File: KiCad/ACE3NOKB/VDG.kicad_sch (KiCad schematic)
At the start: 40 parts, among them Q101 2N3904

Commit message: First complete system. Unlikely to work but will serve as the basis of a system to test VGA.
Signed-off-by: John Bradley <flypie@rocketmail.com>
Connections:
- net INVERTCHAR: now reaches RN1.9 (R8.2), Z20.13, Z5-6.17 (D7)
- net ~{IN_VBI_OR_HBI}: now reaches Z19.4, Z20.12, Z20.6
- net SHIFT/~{LOAD}: now reaches Z19.6, Z28.15 (PE)
- net PIXEL: now reaches Z23.13, Z28.13 (Qh)
- net 50Hz renamed V_SYNC_PULSE(50Hz)
- net ENDOFSCR renamed SCREENY5
- net EOL renamed SCREENX5
- net HSYNC renamed H_SYNC_PULSE
- net SYNCLEVEL renamed ~{SYNC_PULSE}
- net VIDACTIVEONBUS renamed LOAD_SHIFT_REG
- net ~{CPUVDGRAMRD} renamed ~{CPUVDGRD}
- net ~{CPUVDGRAMWR} renamed ~{CPUVDGWR}
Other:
- note added: "END_OF_PIX_V"
- note removed: "50Hz"
- note removed: "VSYNC"
- moved on the sheet: AIN1, C3, D1, D11, Q101, R100, R132, R133, R134, R135, R136, R19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

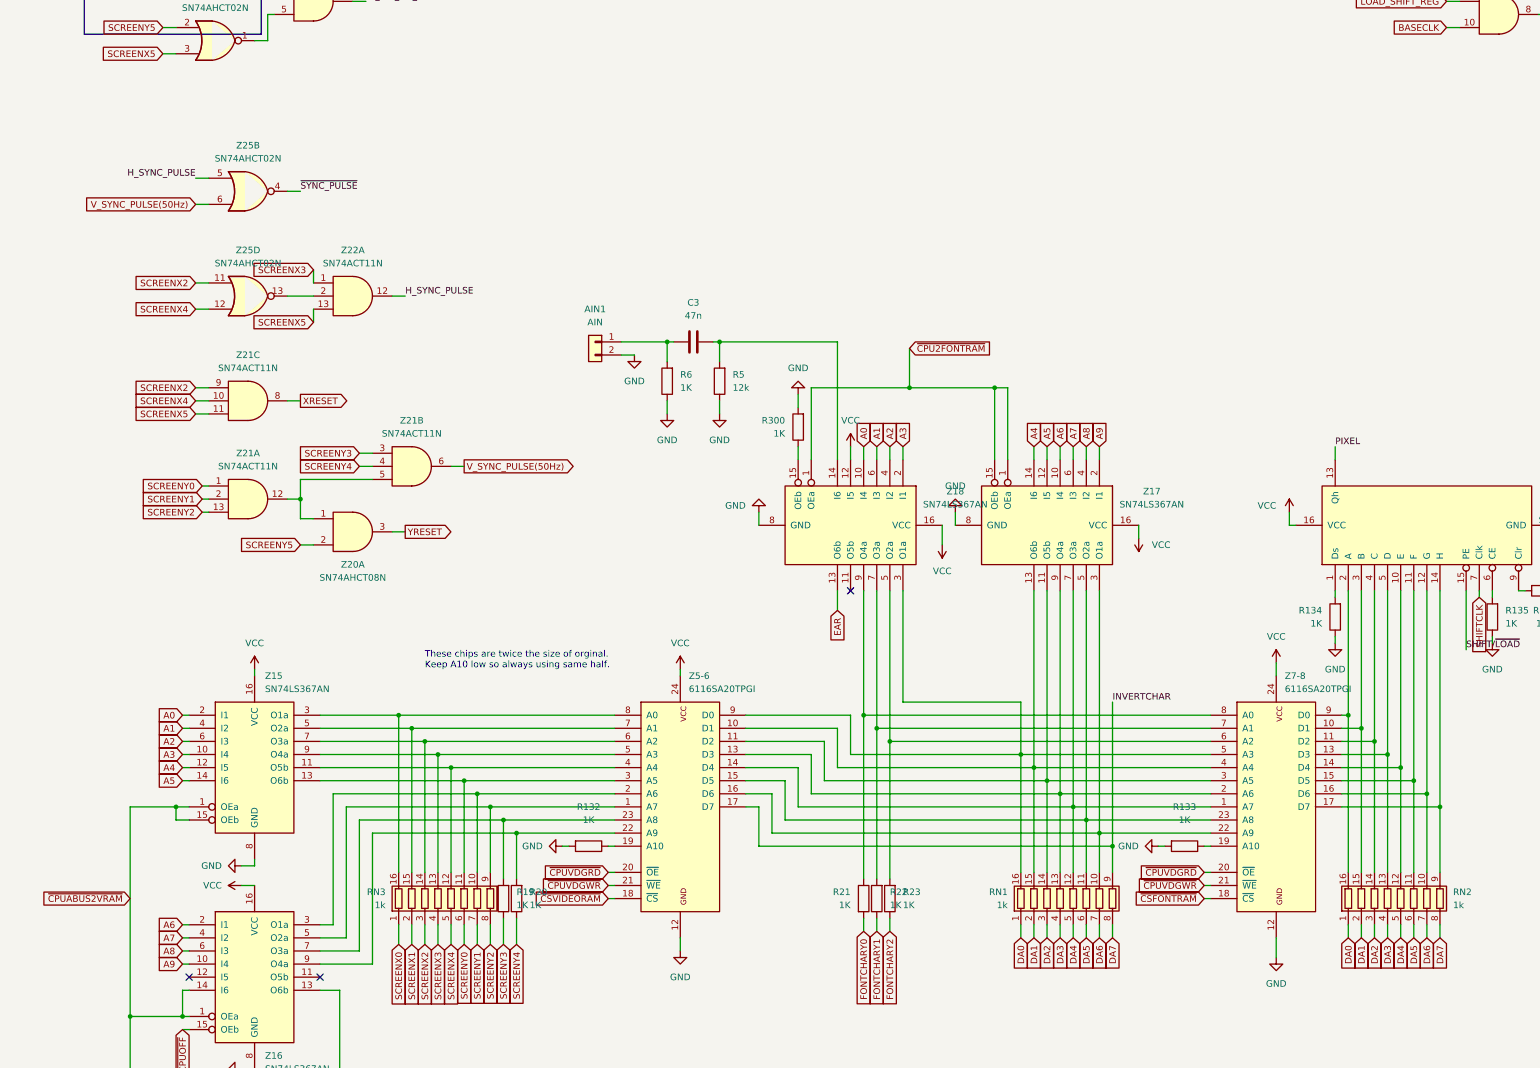
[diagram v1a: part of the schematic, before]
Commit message: Update to latest symbols. Change name of Data Bus from DA to D.
Signed-off-by: John Bradley <flypie@rocketmail.com>
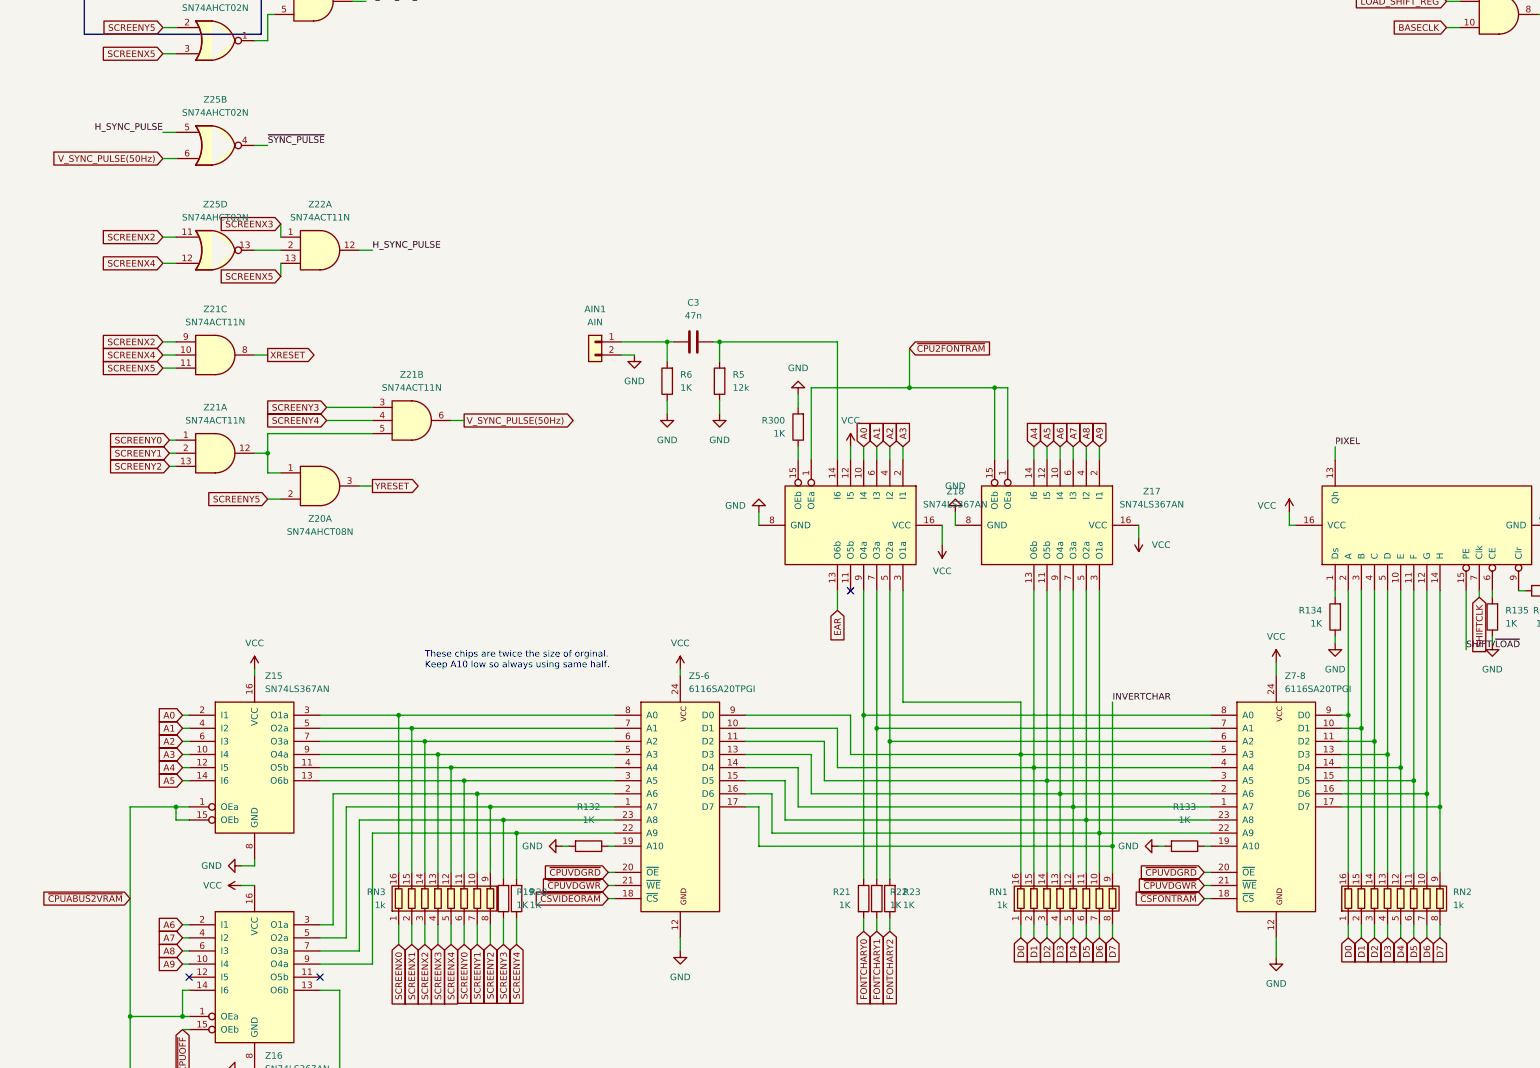
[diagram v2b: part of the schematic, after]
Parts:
- COMP1: footprint ExtraFootprints:PJRAN1X1U03X -> ExtraFootprints:PJRAN1X1U01X
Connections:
- net DA0 renamed D0
- net DA1 renamed D1
- net DA2 renamed D2
- net DA3 renamed D3
- net DA4 renamed D4
- net DA5 renamed D5
- net DA6 renamed D6
- net DA7 renamed D7
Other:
- moved on the sheet: Z20A, Z21A, Z21B, Z21C, Z22A, Z25B, Z25D

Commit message: Consolidation with increased configuration of speed and Int Routing to allow Orginal ACE ROM.
Signed-off-by: John Bradley <flypie@rocketmail.com>
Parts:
- AIN1: Manufacturer_Name TE Connectivity / AMP -> (none); Manufacturer_Part_Number 5-146871-1 -> (none)
- C3: value 47n -> 47nF; Manufacturer_Name vishay -> (none); Manufacturer_Part_Number K473K15X7RF5TL2 -> (none)
- COMP1: value PJRAN1X1U03AUX -> PJRAN1X1U03; Field4 Conn Rca Jack Mono 3.2mm r/a -> (none); Field5 None -> (none); Field6 PJRAN1X1U03AUX -> (none); Field7 Unavailable -> (none); Field8 Switchcraft Inc. -> (none)
- D1, D11: Manufacturer_Name ON Semiconductor -> (none); Manufacturer_Part_Number 1N4148 -> (none)
- Q101: Manufacturer_Part_Number 2N3904 -> (none)
- R100: Manufacturer_Name Vishay -> (none); Manufacturer_Part_Number MBA02040C1000FRP00 -> (none)
- R132, R133, R134, R135, R19, R20, R21, R22, R23, R300, R6: value 1K -> 1K0; Manufacturer_Name Vishay -> (none); Manufacturer_Part_Number MBA02040C1202FRP00 -> (none)
- R136: Manufacturer_Name Vishay -> (none); Manufacturer_Part_Number MBA02040C1002FRP00 -> (none)
- R3, R4: Manufacturer_Name Vishay -> (none); Manufacturer_Part_Number MBA02040C1501FC100 -> (none)
- R5: value 12k -> 12K; Manufacturer_Name Vishay -> (none); Manufacturer_Part_Number MBA02040C1202FRP00 -> (none)
- RN1, RN2, RN3: value 1k -> 1K; Manufacturer_Name Bourns -> (none); Manufacturer_Part_Number 4116R-1-102LF -> (none)
- RV101: Manufacturer_Name Bourns -> (none); Manufacturer_Part_Number 3362H-1-101LF -> (none)
- Z15, Z16, Z17, Z18: Manufacturer_Name Texas Instruments -> (none); Manufacturer_Part_Number SN74LS367AN -> (none)
- Z19: Manufacturer_Name Texas Instruments -> (none); Manufacturer_Part_Number SN74AHCT00N -> (none)
- Z20: Manufacturer_Name Texas Instruments -> (none); Manufacturer_Part_Number SN74AHCT08N -> (none)
- Z21, Z22: Manufacturer_Name Texas Instruments -> (none); Manufacturer_Part_Number SN74ACT11N -> (none)
- Z23: Manufacturer_Name Texas Instruments -> (none); Manufacturer_Part_Number SN74AHCT86N -> (none)
- Z25: value SN74AHCT02N -> SN74AHCT02; Manufacturer_Name Texas Instruments -> (none); Manufacturer_Part_Number SN74AHCT02N -> (none)
- Z27: Manufacturer_Name Texas Instruments -> (none); Manufacturer_Part_Number SN74AHCT74N -> (none)
- Z28: Manufacturer_Name Texas Instruments -> (none); Manufacturer_Part_Number SN74ALS166N -> (none)
- Z5-6, Z7-8: Manufacturer_Name IDT -> (none); Manufacturer_Part_Number 6116SA20TPGI -> (none)
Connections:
- net D0: now also RN1.9 (R8.2), RN2.9 (R8.2); no longer RN1.1 (R1.1), RN2.1 (R1.1)
- net D1: now also RN1.10 (R7.2), RN2.10 (R7.2); no longer RN1.2 (R2.1), RN2.2 (R2.1)
- net D2: now also RN1.11 (R6.2), RN2.11 (R6.2); no longer RN1.3 (R3.1), RN2.3 (R3.1)
- net D3: now also RN1.12 (R5.2), RN2.12 (R5.2); no longer RN1.4 (R4.1), RN2.4 (R4.1)
- net D4: now also RN1.13 (R4.2), RN2.13 (R4.2); no longer RN1.5 (R5.1), RN2.5 (R5.1)
- net D5: now also RN1.14 (R3.2), RN2.14 (R3.2); no longer RN1.6 (R6.1), RN2.6 (R6.1)
- net D6: now also RN1.15 (R2.2), RN2.15 (R2.2); no longer RN1.7 (R7.1), RN2.7 (R7.1)
- net D7: now also RN1.16 (R1.2), RN2.16 (R1.2); no longer RN1.8 (R8.1), RN2.8 (R8.1)
- net GND: now also COMP1.1 (SLEEVE); no longer COMP1.2 (TIP)
- net INVERTCHAR: now also RN1.1 (R1.1); no longer RN1.9 (R8.2)
- net SCREENX0: now also RN3.9 (R8.2); no longer RN3.1 (R1.1)
- net SCREENX1: now also RN3.10 (R7.2); no longer RN3.2 (R2.1)
- net SCREENX2: now also RN3.11 (R6.2); no longer RN3.3 (R3.1)
- net SCREENX3: now also RN3.12 (R5.2); no longer RN3.4 (R4.1)
- net SCREENX4: now also RN3.13 (R4.2); no longer RN3.5 (R5.1)
- net SCREENY0: now also RN3.14 (R3.2); no longer RN3.6 (R6.1)
- net SCREENY1: now also RN3.15 (R2.2); no longer RN3.7 (R7.1)
- net SCREENY2: now also RN3.16 (R1.2); no longer RN3.8 (R8.1)
- net VIDEO: now also Q101.1 (E), R100.1, RV101.1; no longer D1.2 (A), Q101.2 (B), R3.1, R4.2
- net at Z16.5 (O2a), Z5-6.1 (A7): now also RN3.1 (R1.1); no longer RN3.9 (R8.2)
- net at Z17.13 (O6b), Z5-6.10 (D1), Z7-8.4 (A4): now also RN1.7 (R7.1); no longer RN1.15 (R2.2)
- net at Z17.11 (O5b), Z5-6.11 (D2), Z7-8.3 (A5): now also RN1.6 (R6.1); no longer RN1.14 (R3.2)
- net at Z17.9 (O4a), Z5-6.13 (D3), Z7-8.2 (A6): now also RN1.5 (R5.1); no longer RN1.13 (R4.2)
- net at Z17.7 (O3a), Z5-6.14 (D4), Z7-8.1 (A7): now also RN1.4 (R4.1); no longer RN1.12 (R5.2)
- net at Z17.5 (O2a), Z5-6.15 (D5), Z7-8.23 (A8): now also RN1.3 (R3.1); no longer RN1.11 (R6.2)
- net at Z17.3 (O1a), Z5-6.16 (D6), Z7-8.22 (A9): now also RN1.2 (R2.1); no longer RN1.10 (R7.2)
- net at Z16.3 (O1a), Z5-6.2 (A6): now also RN3.2 (R2.1); no longer RN3.10 (R7.2)
- net at Z15.13 (O6b), Z5-6.3 (A5): now also RN3.3 (R3.1); no longer RN3.11 (R6.2)
- net at Z15.11 (O5b), Z5-6.4 (A4): now also RN3.4 (R4.1); no longer RN3.12 (R5.2)
- net at Z15.9 (O4a), Z5-6.5 (A3): now also RN3.5 (R5.1); no longer RN3.13 (R4.2)
- net at Z15.7 (O3a), Z5-6.6 (A2): now also RN3.6 (R6.1); no longer RN3.14 (R3.2)
- net at Z15.5 (O2a), Z5-6.7 (A1): now also RN3.7 (R7.1); no longer RN3.15 (R2.2)
- net at Z15.3 (O1a), Z5-6.8 (A0): now also RN3.8 (R8.1); no longer RN3.16 (R1.2)
- net at Z18.3 (O1a), Z5-6.9 (D0), Z7-8.5 (A3): now also RN1.8 (R8.1); no longer RN1.16 (R1.2)
- net VD1: now reaches Z28.3 (B), Z7-8.10 (D1)
- net VD1: now also RN2.7 (R7.1); no longer RN2.15 (R2.2)
- net VD2: now reaches Z28.4 (C), Z7-8.11 (D2)
- net VD2: now also RN2.6 (R6.1); no longer RN2.14 (R3.2)
- net VD3: now reaches Z28.5 (D), Z7-8.13 (D3)
- net VD3: now also RN2.5 (R5.1); no longer RN2.13 (R4.2)
- net VD4: now reaches Z28.10 (E), Z7-8.14 (D4)
- net VD4: now also RN2.4 (R4.1); no longer RN2.12 (R5.2)
- net VD5: now reaches Z28.11 (F), Z7-8.15 (D5)
- net VD5: now also RN2.3 (R3.1); no longer RN2.11 (R6.2)
- net VD6: now reaches Z28.12 (G), Z7-8.16 (D6)
- net VD6: now also RN2.2 (R2.1); no longer RN2.10 (R7.2)
- net VD7: now reaches Z28.14 (H), Z7-8.17 (D7)
- net VD7: now also RN2.1 (R1.1); no longer RN2.9 (R8.2)
- net VD0: now reaches Z28.2 (A), Z7-8.9 (D0)
- net VD0: now also RN2.8 (R8.1); no longer RN2.16 (R1.2)
- net at RV101.2: now also COMP1.2 (TIP); no longer COMP1.1 (SLEEVE)
- net ~{CPUABUS2VRAM} renamed ~{CPU2VIDEORAM}
- net ~{CSFONTRAM} renamed ~{FONTRAMCS}
- net ~{CSVIDEORAM} renamed ~{VIDEORAMCS}
- net ~{VIDHOLDCPUOFF} renamed ~{VDGHASPRIORITY}
- new net RAWVIDEO: D1.2 (A), Q101.2 (B), R3.1, R4.2
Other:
- note added: "If ~{CPU2VIDEORAM} goes high while ~{VDGHASPRIORITY} is low the diode is kept high until ~{VDGHASPRIORITY} goes high. DIODE ensures only pulls high."
- moved on the sheet: AIN1, C3, D1, D11, Q101, R100, R132, R133, R134, R135, R136, R19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
